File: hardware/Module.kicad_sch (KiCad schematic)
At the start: 121 parts, among them SW2 Encoder

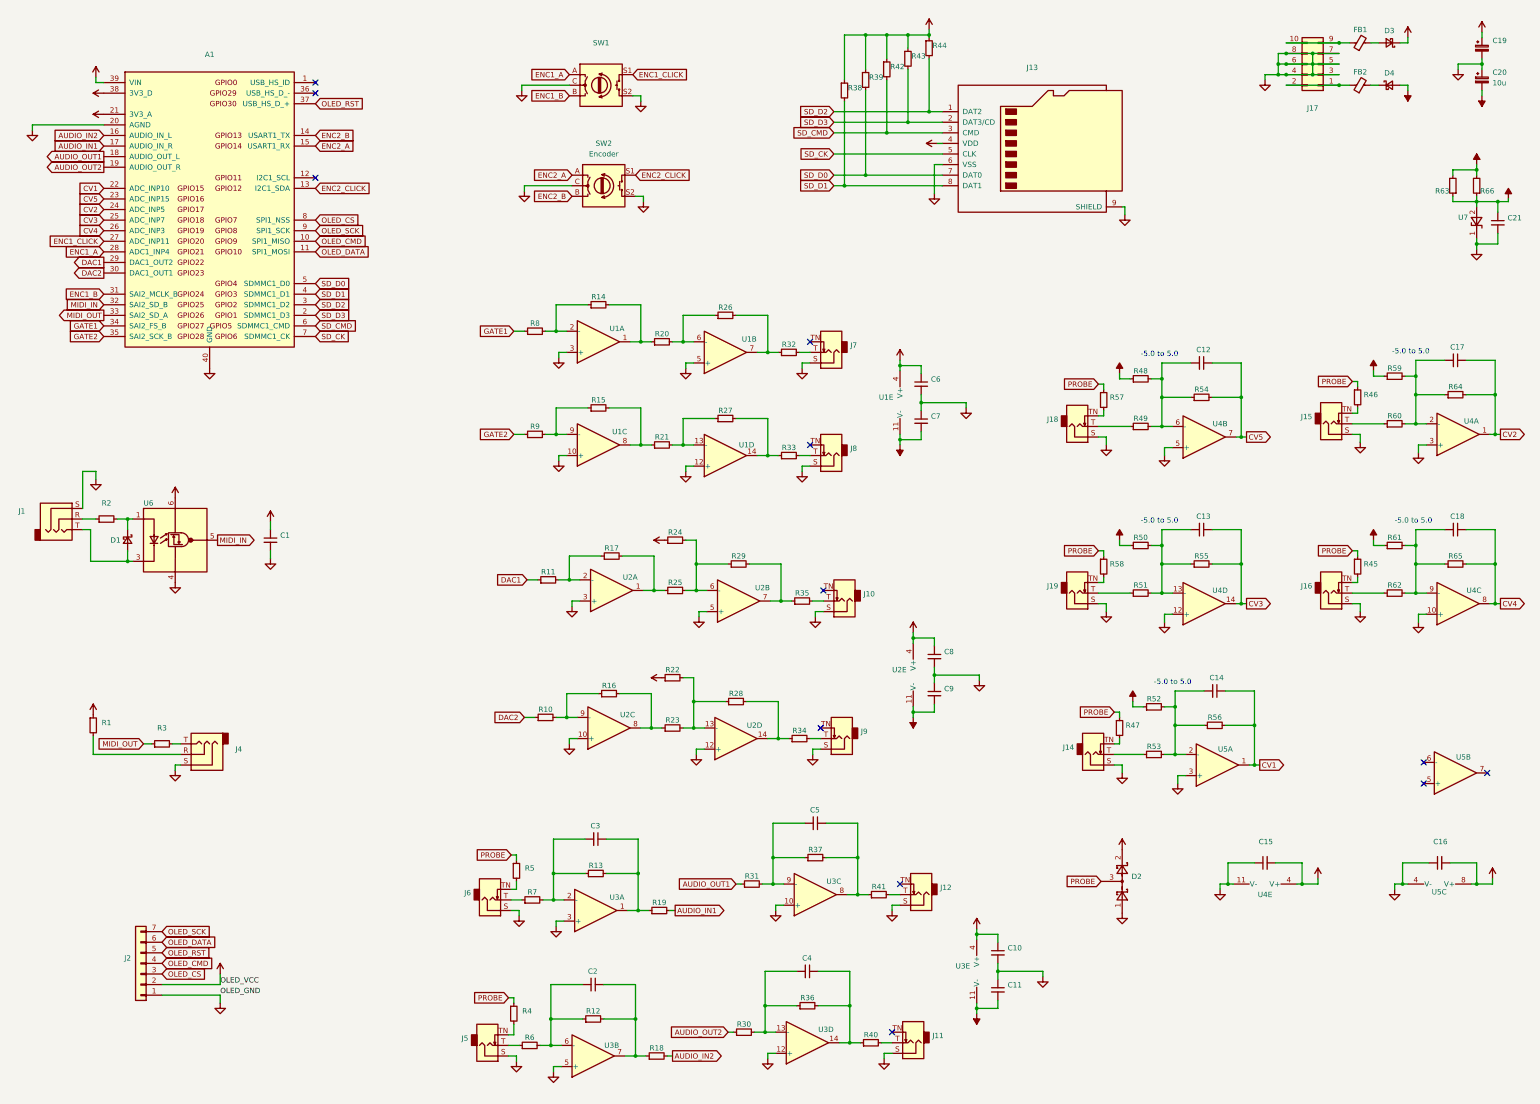
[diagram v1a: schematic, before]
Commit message: hw: Describe issues with OLED mapping
Signed-off-by: Petr Horacek <hrck@protonmail.com>
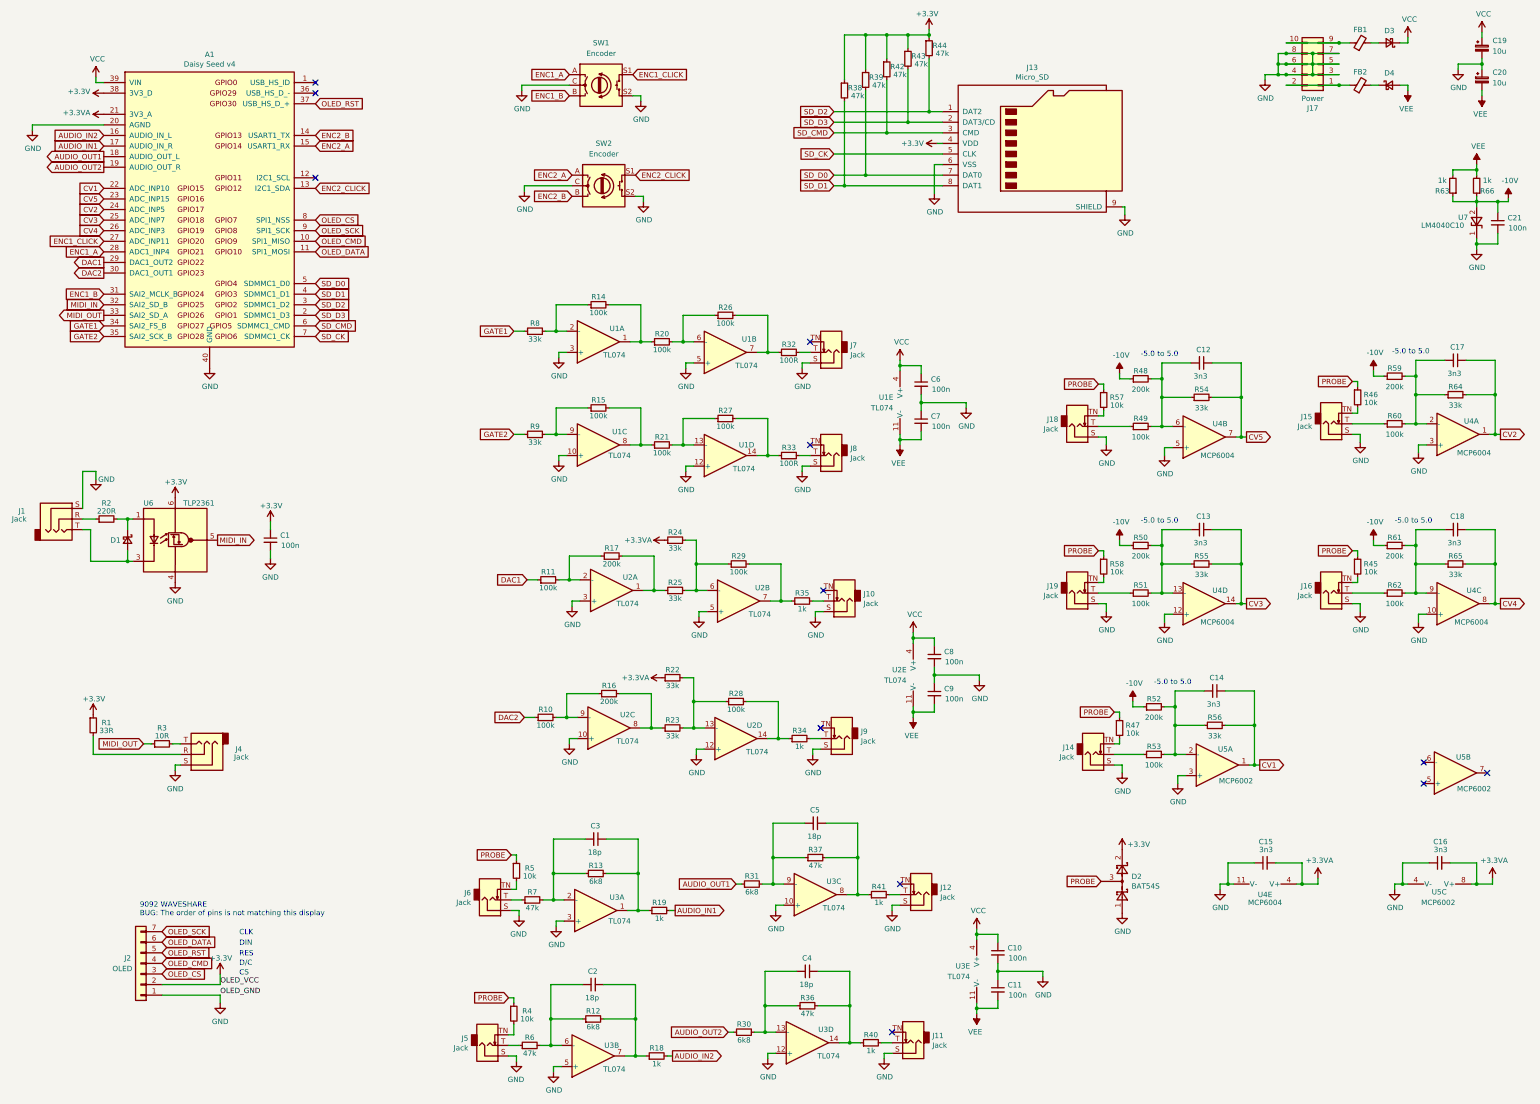
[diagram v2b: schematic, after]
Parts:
- A1: value (none) -> Daisy Seed v4; footprint (none) -> Device_Audio_Electrosmith_Daisy_Seed:Device_Audio_Electrosmith_Daisy_Seed
- C1, C10, C11, C21, C6, C7, C8, C9: value (none) -> 100n; footprint (none) -> Capacitor_SMD:C_0603_1608Metric_Pad1.08x0.95mm_HandSolder
- C12, C13, C14, C15, C16, C17, C18: value (none) -> 3n3; footprint (none) -> Capacitor_SMD:C_0603_1608Metric_Pad1.08x0.95mm_HandSolder
- C19: value (none) -> 10u; footprint (none) -> Capacitor_SMD:CP_Elec_6.3x5.8
- C2, C3, C4, C5: value (none) -> 18p; footprint (none) -> Capacitor_SMD:C_0603_1608Metric_Pad1.08x0.95mm_HandSolder
- D1, D3, D4: value (none) -> Schottky; footprint (none) -> Diode_SMD:D_SOD-123
- D2: value (none) -> BAT54S; footprint (none) -> Package_TO_SOT_SMD:SOT-23_Handsoldering
- FB1: value (none) -> FB; footprint (none) -> Inductor_SMD:L_0603_1608Metric_Pad1.05x0.95mm_HandSolder
- J1, J4: value (none) -> Jack; footprint (none) -> Custom:Jack_3.5mm_QingPu_WQP-PJ398SM_Vertical_CircularHoles_Stereo
- J10, J11, J12, J14, J15, J16, J18, J19, J5, J6, J7, J8, J9: value (none) -> Jack; footprint (none) -> Connector_Audio:Jack_3.5mm_QingPu_WQP-PJ398SM_Vertical_CircularHoles
- J13: value (none) -> Micro_SD; footprint (none) -> Custom:microsd_connector
- J17: value (none) -> Power; footprint (none) -> Connector_PinHeader_2.54mm:PinHeader_2x05_P2.54mm_Vertical
- J2: value (none) -> OLED; footprint (none) -> Connector_PinSocket_2.54mm:PinSocket_1x07_P2.54mm_Vertical
- R1: value (none) -> 33R; footprint (none) -> Resistor_SMD:R_0603_1608Metric_Pad0.98x0.95mm_HandSolder
- R10, R11, R14, R15, R20, R21, R26, R27, R28, R29, R49, R51, R53, R60, R62: value (none) -> 100k; footprint (none) -> Resistor_SMD:R_0603_1608Metric_Pad0.98x0.95mm_HandSolder
- R12, R13, R30, R31: value (none) -> 6k8; footprint (none) -> Resistor_SMD:R_0603_1608Metric_Pad0.98x0.95mm_HandSolder
- R16, R17, R48, R50, R52, R59, R61: value (none) -> 200k; footprint (none) -> Resistor_SMD:R_0603_1608Metric_Pad0.98x0.95mm_HandSolder
- R18, R19, R34, R35, R40, R41, R63, R66: value (none) -> 1k; footprint (none) -> Resistor_SMD:R_0603_1608Metric_Pad0.98x0.95mm_HandSolder
- R2: value (none) -> 220R; footprint (none) -> Resistor_SMD:R_0603_1608Metric_Pad0.98x0.95mm_HandSolder
- R22, R23, R24, R25, R54, R55, R56, R64, R65, R8, R9: value (none) -> 33k; footprint (none) -> Resistor_SMD:R_0603_1608Metric_Pad0.98x0.95mm_HandSolder
- R3: value (none) -> 10R; footprint (none) -> Resistor_SMD:R_0603_1608Metric_Pad0.98x0.95mm_HandSolder
- R32, R33: value (none) -> 100R; footprint (none) -> Resistor_SMD:R_0603_1608Metric_Pad0.98x0.95mm_HandSolder
- R36, R37, R38, R39, R42, R43, R44, R6, R7: value (none) -> 47k; footprint (none) -> Resistor_SMD:R_0603_1608Metric_Pad0.98x0.95mm_HandSolder
- R4, R45, R46, R47, R5, R57, R58: value (none) -> 10k; footprint (none) -> Resistor_SMD:R_0603_1608Metric_Pad0.98x0.95mm_HandSolder
- SW1: value (none) -> Encoder; footprint (none) -> Rotary_Encoder:RotaryEncoder_Alps_EC11E-Switch_Vertical_H20mm
- U1, U2, U3: value (none) -> TL074; footprint (none) -> Package_SO:SOIC-14_3.9x8.7mm_P1.27mm
- U4: value (none) -> MCP6004; footprint (none) -> Package_SO:SOIC-14_3.9x8.7mm_P1.27mm
- U5: value (none) -> MCP6002; footprint (none) -> Package_SO:SOIC-8_3.9x4.9mm_P1.27mm
- U6: value (none) -> TLP2361; footprint (none) -> Package_SO:SO-6L_10x3.84mm_P1.27mm
- U7: value (none) -> LM4040C10; footprint (none) -> Package_TO_SOT_SMD:SOT-23_Handsoldering
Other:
- note added: "9092 WAVESHARE BUG: The order of pins is not matching this display"
- note added: "CLK"
- note added: "CS"
- note added: "D/C"
- note added: "DIN"
- note added: "RES"

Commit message: Place THT on two-layer PCB
Signed-off-by: Petr Horacek <hrck@protonmail.com>
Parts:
- removed C1: 100n, Capacitor_SMD:C_0603_1608Metric_Pad1.08x0.95mm_HandSolder, symbol Device:C_Small
- removed D1: Schottky, Diode_SMD:D_SOD-123, symbol Device:D_Schottky_Small
- removed J1, J4: Jack, Custom:Jack_3.5mm_QingPu_WQP-PJ398SM_Vertical_CircularHoles_Stereo, symbol Connector:AudioJack3
- removed J14: Jack, Connector_Audio:Jack_3.5mm_QingPu_WQP-PJ398SM_Vertical_CircularHoles, symbol Connector:AudioJack2_SwitchT
- removed R21, R26, R27: 100k, Resistor_SMD:R_0603_1608Metric_Pad0.98x0.95mm_HandSolder, symbol Device:R_Small
- removed R33: 100R, Resistor_SMD:R_0603_1608Metric_Pad0.98x0.95mm_HandSolder, symbol Device:R_Small
- removed SW2: Encoder, Rotary_Encoder:RotaryEncoder_Alps_EC11E-Switch_Vertical_H20mm, symbol Device:RotaryEncoder_Switch
- removed U6: TLP2361, Package_SO:SO-6L_10x3.84mm_P1.27mm, symbol Isolator:TLP2761
- added J1, J4: Jack, Connector_Audio:Jack_3.5mm_QingPu_WQP-PJ398SM_Vertical_CircularHoles, symbol Connector:AudioJack2_SwitchT
- added J14, J21, J3: Conn_02x08_Odd_Even, Connector_PinSocket_2.54mm:PinSocket_2x08_P2.54mm_Vertical, symbol Connector_Generic:Conn_02x08_Odd_Even
- added J20, J22, J23: Conn_02x08_Odd_Even, Connector_PinHeader_2.54mm:PinHeader_2x08_P2.54mm_Vertical, symbol Connector_Generic:Conn_02x08_Odd_Even
- added RV1: Pot, Potentiometer_THT:Potentiometer_Alpha_RD901F-40-00D_Single_Vertical, symbol Device:R_Potentiometer
- R1: value 33R -> 33k; LCSC C25744 -> C23212; Mfr Part Number CR0603-FX-1002ELF -> CR0603-JW-682ELF
- R15: value 100k -> 100R; LCSC C25819 -> C21190; Mfr Part Number CR0603-FX-4702ELF -> CR0603-FX-1001ELF
- R2: value 220R -> 33k; LCSC C25819 -> C23212; Mfr Part Number CR0603-FX-4702ELF -> CR0603-JW-682ELF
- R20: value 100k -> 100R; LCSC C23212 -> C21190; Mfr Part Number CR0603-JW-682ELF -> CR0603-FX-1001ELF
- R3: value 10R -> 100k
- R9: value 33k -> 100k; LCSC C23212 -> C25819; Mfr Part Number CR0603-JW-682ELF -> CR0603-FX-4702ELF
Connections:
- net +3.3VA: now also RV1.3
- net +3V3: no longer R1.1
- net GATE1: now also U1.3 (+); no longer R8.1
- net GATE2: now also U1.6 (-); no longer R9.1
- net GND: now also R1.1, R2.1, R8.1, J1.S, J4.S, RV1.1; no longer U1.10 (+), U1.12 (+), U1.3 (+), U1.5 (+)
- net OLED_CMD: now also J2.6 (Pin_6); no longer J2.4 (Pin_4)
- net OLED_CS: now also J2.7 (Pin_7); no longer J2.3 (Pin_3)
- net OLED_DATA: now also J2.4 (Pin_4); no longer J2.6 (Pin_6)
- net OLED_SCK: now also J2.3 (Pin_3); no longer J2.7 (Pin_7)
- net at J11.T: now also R49.1; no longer R40.2
- net at J11.TN: now also R57.2
- net at J12.T: now also R62.1; no longer R41.2
- net at J12.TN: now also R45.2
- net at J16.T: now also R40.2; no longer R62.1
- net at J16.TN: no longer R45.2
- net at J15.T: now also R6.1; no longer R60.1
- net at J15.TN: now also R4.2; no longer R46.2
- net at J19.T: now also R41.2; no longer R51.1
- net at J19.TN: no longer R58.2
- net at J18.T: now also R7.1; no longer R49.1
- net at J18.TN: now also R5.2; no longer R57.2
- net at R53.1: now also J4.T
- net at R47.2: now also J4.TN
- net at J5.TN: now also R58.2; no longer R4.2
- net at R14.2, U1.1: now also R32.1; no longer R20.1
- net at R20.2: now also J7.T; no longer U1.6 (-)
- net at U1.7: now also R20.1, R9.2; no longer R32.1
- net at R32.2: now also J1.T; no longer J7.T
- net at R1.2: now also R3.1, U1.10 (+)
- net at R3.2: now also R15.1, U1.8
- net at R15.2: now also J8.T; no longer U1.8
- net at J5.T: now also R51.1; no longer R6.1
- net at J6.T: now also R60.1; no longer R7.1
- net at J6.TN: now also R46.2; no longer R5.2
- net at R2.2: now also R9.1, U1.5 (+)
- net ENC1_A renamed ENC_A
- net ENC1_B renamed ENC_B
- net ENC1_CLICK renamed ENC_CLICK
- net ENC2_A: no longer names the net of A1.15 (USART1_RX)
- net ENC2_B: no longer names the net of A1.14 (USART1_TX)
- net ENC2_CLICK: no longer names the net of A1.13 (I2C1_SDA)
- net MIDI_IN: no longer names the net of A1.32 (SAI2_SD_B)
- net MIDI_OUT: no longer names the net of A1.33 (SAI2_SD_A)
- net MIDI_OUT: no longer R3.1
- new net GATE3: U1.9 (-)
- new net POT: RV1.2
- no-connect marks 12 -> 16
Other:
- note added: "0.96" OLED from Thonk https://www.thonk.co.uk/shop/0-96-oled-screen-vcmc-cv-thing/"
- note removed: "9092 WAVESHARE BUG: The order of pins is not matching this display"
- moved on the sheet: A1, C10, C11, C12, C13, C14, C15, C16, C17, C18, C19, C2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

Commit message: Wire up all connections
Signed-off-by: Petr Horacek <hrck@protonmail.com>
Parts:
- removed J14, J21, J3: Conn_02x08_Odd_Even, Connector_PinSocket_2.54mm:PinSocket_2x08_P2.54mm_Vertical, symbol Connector_Generic:Conn_02x08_Odd_Even
- removed J20, J22, J23: Conn_02x08_Odd_Even, Connector_PinHeader_2.54mm:PinHeader_2x08_P2.54mm_Vertical, symbol Connector_Generic:Conn_02x08_Odd_Even
- added J14: NW_B, Connector_PinSocket_2.54mm:PinSocket_2x06_P2.54mm_Vertical, symbol Connector_Generic:Conn_02x06_Odd_Even
- added J20: SW_B, Connector_PinSocket_2.54mm:PinSocket_2x06_P2.54mm_Vertical, symbol Connector_Generic:Conn_02x06_Odd_Even
- added J21: NW_A, Connector_PinHeader_2.54mm:PinHeader_2x06_P2.54mm_Vertical, symbol Connector_Generic:Conn_02x06_Odd_Even
- added J22: SW_A, Connector_PinHeader_2.54mm:PinHeader_2x06_P2.54mm_Vertical, symbol Connector_Generic:Conn_02x06_Odd_Even
- added J23: NE_A, Connector_PinHeader_2.54mm:PinHeader_2x06_P2.54mm_Vertical, symbol Connector_Generic:Conn_02x06_Odd_Even
- added J3: NE_B, Connector_PinSocket_2.54mm:PinSocket_2x06_P2.54mm_Vertical, symbol Connector_Generic:Conn_02x06_Odd_Even
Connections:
- net +3.3VA: now also J14.10 (Pin_10), J21.10 (Pin_10)
- net +3V3: now also J23.1 (Pin_1), J3.1 (Pin_1)
- net GATE3: now also A1.36 (USB_HS_D_-)
- net AUDIO_OUT1_JACK_A: now reaches C5.1, R37.2, U3.8
- net AUDIO_OUT1_JACK_A: now also J22.1 (Pin_1); no longer R41.1
- net AUDIO_OUT2_JACK_A: now reaches C4.1, R36.2, U3.14
- net AUDIO_OUT2_JACK_A: now also J22.3 (Pin_3); no longer R40.1
- net GATE1_JACK_A: now reaches R14.2, U1.1
- net GATE1_JACK_A: now also J22.7 (Pin_7); no longer R32.1
- net PROBE_A: now reaches A1.32 (SAI2_SD_B)
- net PROBE_A: now also D2.3, J23.12 (Pin_12)
- net ENC_CLICK_A: now reaches A1.33 (SAI2_SD_A)
- net ENC_CLICK_A: now also J21.9 (Pin_9)
- net GATE3_JACK_A: now reaches R3.2, U1.8
- net GATE3_JACK_A: now also J22.5 (Pin_5); no longer R15.1
- net GATE2_JACK_A: now reaches R9.2, U1.7
- net GATE2_JACK_A: now also J22.6 (Pin_6); no longer R20.1
- net AUDIO_IN2_JACK_A: now reaches C2.2, R12.1, U3.6 (-)
- net AUDIO_IN2_JACK_A: now also J22.8 (Pin_8); no longer R6.2
- net AUDIO_IN1_JACK_A: now reaches C3.2, R13.1, U3.2 (-)
- net AUDIO_IN1_JACK_A: now also J22.9 (Pin_9); no longer R7.2
- net DAC1_JACK_A: now reaches R29.2, U2.7
- net DAC1_JACK_A: now also J22.4 (Pin_4); no longer R35.1
- net DAC2_JACK_A: now reaches R28.2, U2.14
- net DAC2_JACK_A: now also J22.2 (Pin_2); no longer R34.1
- net CV1 renamed CV1_B
- net CV1_B: now also J3.10 (Pin_10); no longer A1.22 (ADC_INP10)
- net CV2 renamed CV2_B
- net CV2_B: now also J3.4 (Pin_4); no longer A1.24 (ADC_INP5)
- net CV3 renamed CV3_B
- net CV3_B: now also J3.8 (Pin_8); no longer A1.25 (ADC_INP7)
- net CV4 renamed CV4_B
- net CV4_B: now also J3.6 (Pin_6); no longer A1.26 (ADC_INP3)
- net CV5 renamed CV5_B
- net CV5_B: now also J3.2 (Pin_2); no longer A1.23 (ADC_INP15)
- net ENC_A renamed ENC_A_A
- net ENC_A_A: now also J21.11 (Pin_11); no longer SW1.A
- net ENC_B renamed ENC_B_A
- net ENC_B_A: now also J21.12 (Pin_12); no longer SW1.B
- net ENC_CLICK renamed ENC_CLICK_B
- net ENC_CLICK_B: now also J14.9 (Pin_9); no longer A1.27 (ADC_INP11)
- net OLED_CMD renamed OLED_CMD_A
- net OLED_CMD_A: now also J23.5 (Pin_5); no longer J2.6 (Pin_6)
- net OLED_CS renamed OLED_CS_A
- net OLED_CS_A: now also J23.3 (Pin_3); no longer J2.7 (Pin_7)
- net OLED_DATA renamed OLED_DATA_A
- net OLED_DATA_A: now also J23.9 (Pin_9); no longer J2.4 (Pin_4)
- net OLED_RST renamed OLED_RST_A
- net OLED_RST_A: now also J23.7 (Pin_7); no longer J2.5 (Pin_5)
- net OLED_SCK renamed OLED_SCK_A
- net OLED_SCK_A: now also J23.11 (Pin_11); no longer J2.3 (Pin_3)
- net POT renamed POT_B
- net POT_B: now also J20.10 (Pin_10)
- net PROBE renamed PROBE_B
- net PROBE_B: now also J3.12 (Pin_12); no longer D2.3
- net SD_CK renamed SD_CK_A
- net SD_CK_A: now also J21.3 (Pin_3); no longer J13.5 (CLK)
- net SD_CMD renamed SD_CMD_B
- net SD_CMD_B: now also J14.4 (Pin_4); no longer A1.6 (SDMMC1_CMD)
- net SD_D0 renamed SD_D0_B
- net SD_D0_B: now also J14.2 (Pin_2); no longer A1.5 (SDMMC1_D0)
- net SD_D1 renamed SD_D1_B
- net SD_D1_B: now also J14.1 (Pin_1); no longer A1.4 (SDMMC1_D1)
- net SD_D2 renamed SD_D2_B
- net SD_D2_B: now also J14.6 (Pin_6); no longer A1.3 (SDMMC1_D2)
- net SD_D3 renamed SD_D3_B
- net SD_D3_B: now also J14.5 (Pin_5); no longer A1.2 (SDMMC1_D3)
- new net AUDIO_IN1_JACK_B: J20.9 (Pin_9), R7.2
- new net AUDIO_IN2_JACK_B: J20.8 (Pin_8), R6.2
- new net AUDIO_OUT1_JACK_B: J20.1 (Pin_1), R41.1
- new net AUDIO_OUT2_JACK_B: J20.3 (Pin_3), R40.1
- new net CV1_A: A1.22 (ADC_INP10), J23.10 (Pin_10)
- new net CV2_A: A1.24 (ADC_INP5), J23.4 (Pin_4)
- new net CV3_A: A1.25 (ADC_INP7), J23.8 (Pin_8)
- new net CV4_A: A1.26 (ADC_INP3), J23.6 (Pin_6)
- new net CV5_A: A1.23 (ADC_INP15), J23.2 (Pin_2)
- new net DAC1_JACK_B: J20.4 (Pin_4), R35.1
- new net DAC2_JACK_B: J20.2 (Pin_2), R34.1
- new net ENC_A_B: J14.11 (Pin_11), SW1.A
- new net ENC_B_B: J14.12 (Pin_12), SW1.B
- new net GATE1_JACK_B: J20.7 (Pin_7), R32.1
- new net GATE2_JACK_B: J20.6 (Pin_6), R20.1
- new net GATE3_JACK_B: J20.5 (Pin_5), R15.1
- new net OLED_CMD_B: J2.6 (Pin_6), J3.5 (Pin_5)
- new net OLED_CS_B: J2.7 (Pin_7), J3.3 (Pin_3)
- new net OLED_DATA_B: J2.4 (Pin_4), J3.9 (Pin_9)
- new net OLED_RST_B: J2.5 (Pin_5), J3.7 (Pin_7)
- new net OLED_SCK_B: J2.3 (Pin_3), J3.11 (Pin_11)
- new net POT_A: A1.27 (ADC_INP11), J22.10 (Pin_10)
- new net SD_CK_B: J13.5 (CLK), J14.3 (Pin_3)
- new net SD_CMD_A: A1.6 (SDMMC1_CMD), J21.4 (Pin_4)
- new net SD_D0_A: A1.5 (SDMMC1_D0), J21.2 (Pin_2)
- new net SD_D1_A: A1.4 (SDMMC1_D1), J21.1 (Pin_1)
- new net SD_D2_A: A1.3 (SDMMC1_D2), J21.6 (Pin_6)
- new net SD_D3_A: A1.2 (SDMMC1_D3), J21.5 (Pin_5)
- no-connect marks 16 -> 15
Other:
- note added: "TODO: Confirm that all globals are connected"
- moved on the sheet: C10, C11, C12, C13, C14, C2, C3, C4, C5, C6, C7, C8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
